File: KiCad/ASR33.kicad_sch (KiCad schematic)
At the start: 45 parts, among them J1 USB-C, J2 DC, J3 Power, J4 RUN, J5 Tx, J6 Rx, Q1 NX7002AK, SW1 SW_Push, U1 ESP32-WROOM-32, U2 FT231XQ, U3 NCR402U, U4 NCR402U, U5 LTV-356T, U6 LMR16006+FB, U7 QR

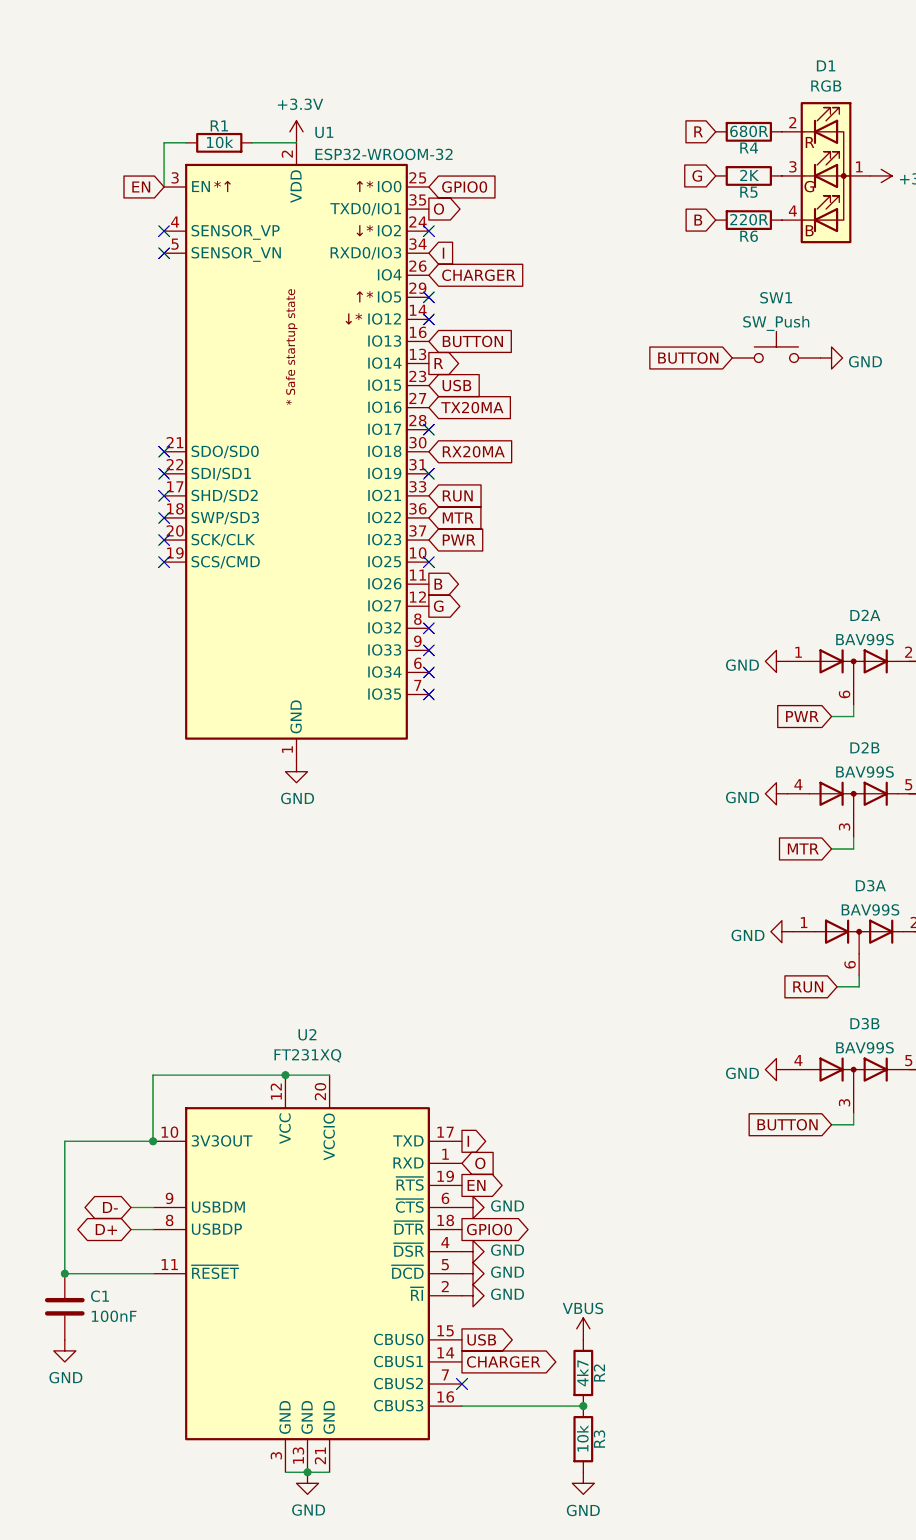
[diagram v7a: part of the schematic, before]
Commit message: FFS, missed 3.3V to FT231XQ
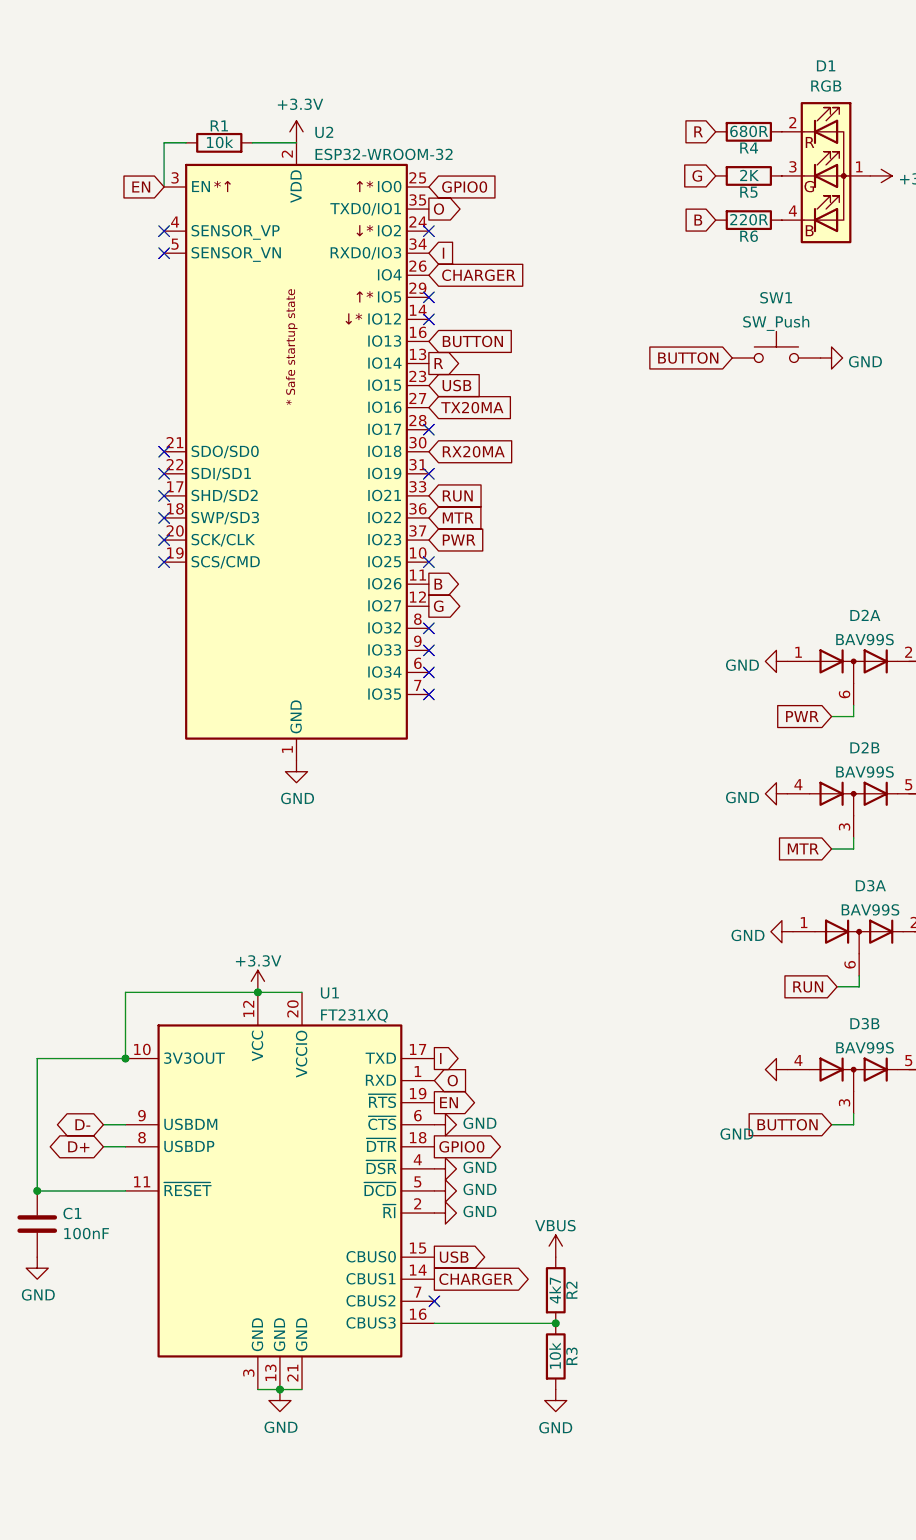
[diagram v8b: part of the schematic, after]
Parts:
- removed U2: FT231XQ, Package_DFN_QFN:QFN-20-1EP_4x4mm_P0.5mm_EP2.5x2.5mm, symbol Interface_USB:FT231XQ
- added U1: FT231XQ, RevK:QFN-20-1EP_4x4mm_P0.5mm_EP2.5x2.5mm, symbol RevK:FT231XQ
- renumbered U1 to U2
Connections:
- net +3V3: now also C1.1, U1.10 (3V3OUT), U1.11 (~{RESET}), U1.12 (VCC), U1.20 (VCCIO)
- net CHARGER: now also U1.14 (CBUS1)
- net D+: now also U1.8 (USBDP)
- net D-: now also U1.9 (USBDM)
- net EN: now also U1.19 (~{RTS})
- net GND: now also U1.13 (GND), U1.2 (~{RI}), U1.21 (GND), U1.3 (GND), U1.4 (~{DSR}), U1.5 (~{DCD}), U1.6 (~{CTS})
- net GPIO0: now also U1.18 (~{DTR})
- net I: now also U1.17 (TXD)
- net O: now also U1.1 (RXD)
- net USB: now also U1.15 (CBUS0)
- net at R2.2, R3.1: now also U1.16 (CBUS3)
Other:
- moved on the sheet: C1, R2, R3
